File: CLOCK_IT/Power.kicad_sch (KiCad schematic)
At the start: 38 parts, among them SW1 CK_KMS2xxG, U4 AXP2101, U5 MC-264, U6 DS1338Z-NF, Y2 ABS07-32.768KHZ-T

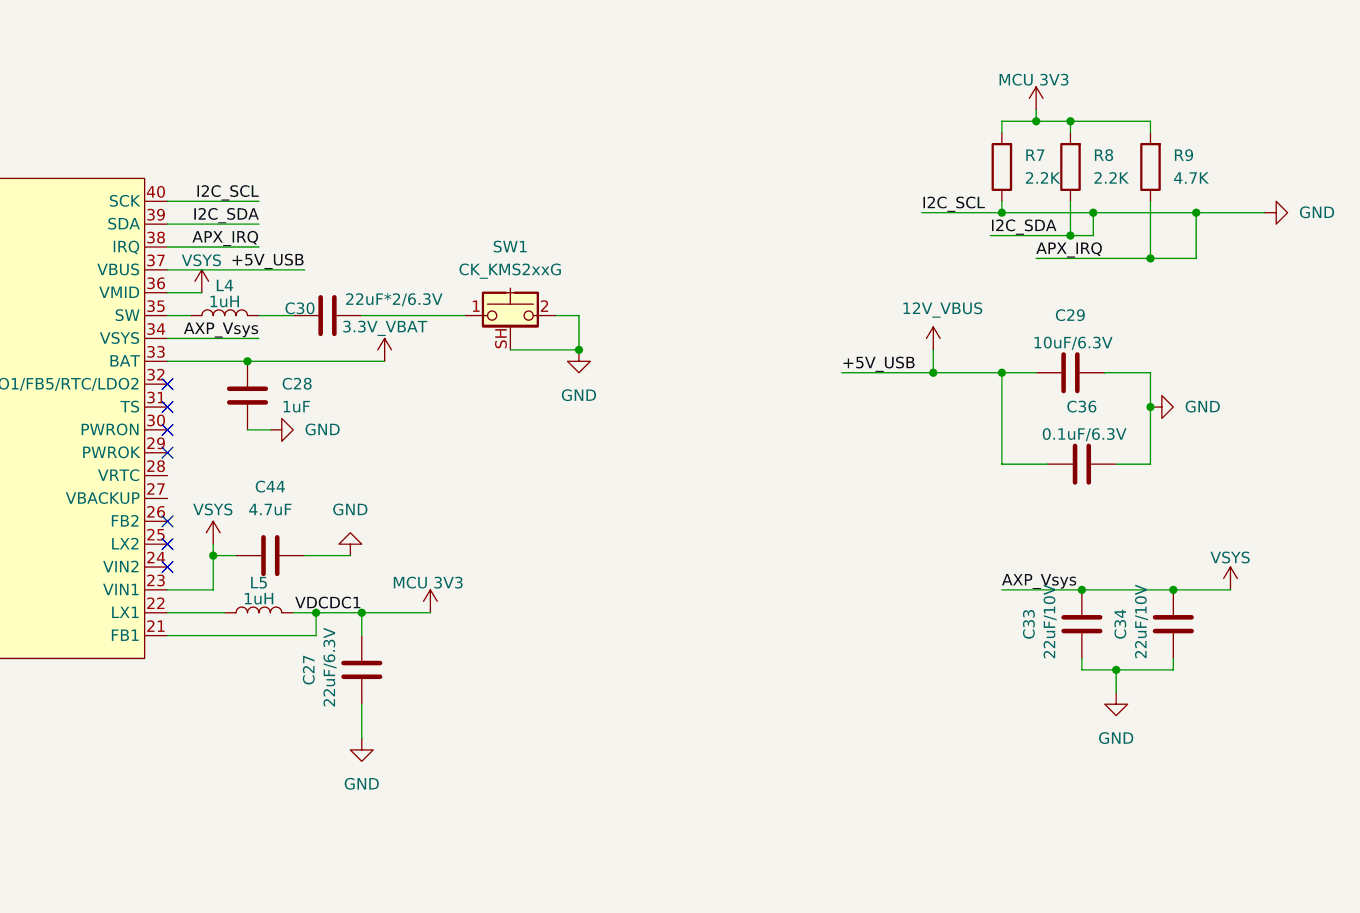
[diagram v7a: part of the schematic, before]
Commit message: :white_check_mark: CHANGES in 12C pull up resisors
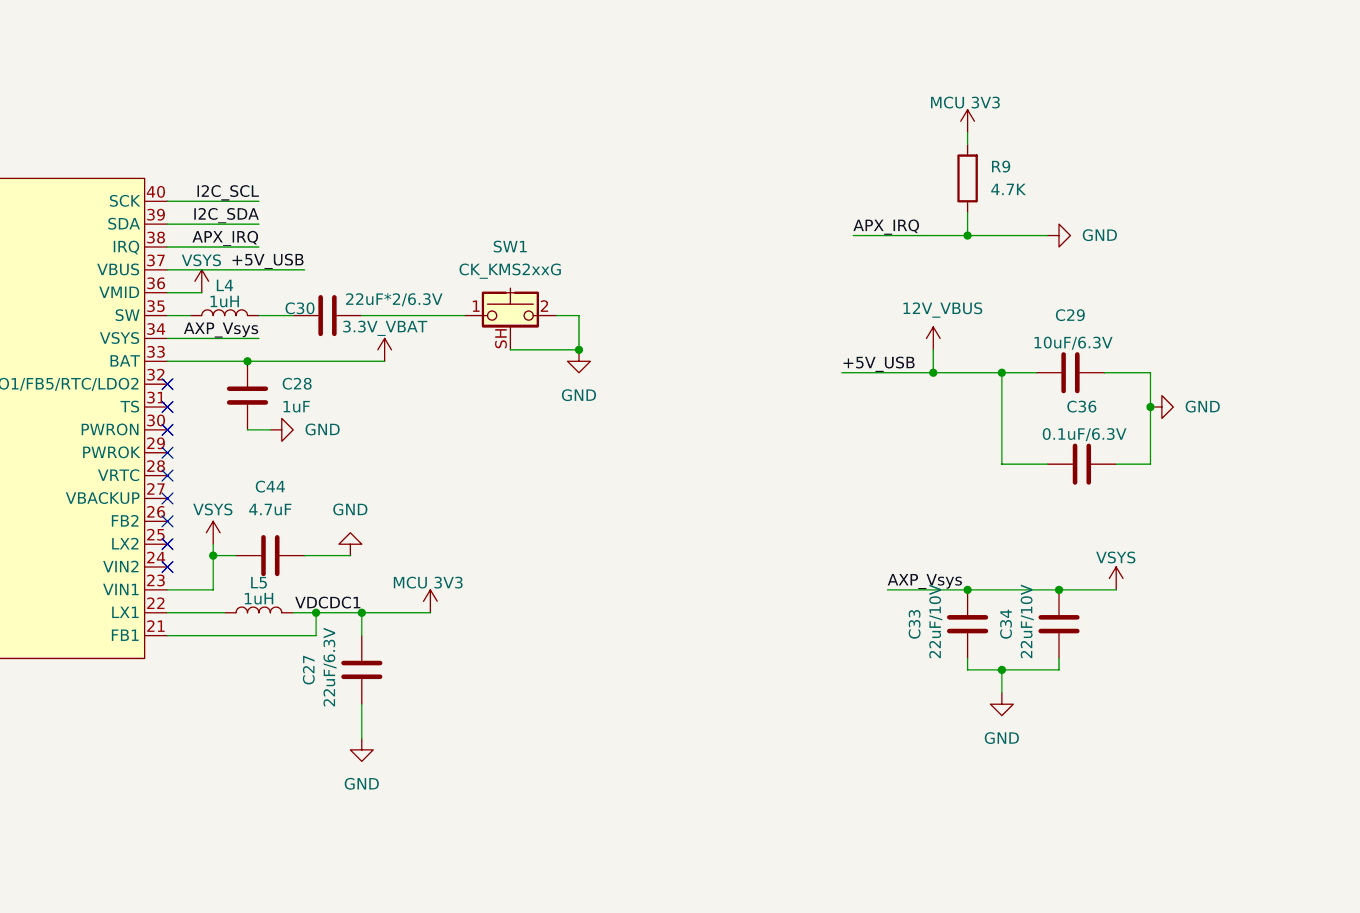
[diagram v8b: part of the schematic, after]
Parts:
- removed R7, R8: 2.2K, symbol Device:R
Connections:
- net GND: no longer U4.39 (SDA), U4.40 (SCK)
- new net I2C_SCL: U4.40 (SCK)
- new net I2C_SDA: U4.39 (SDA)
- no-connect marks 25 -> 27
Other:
- moved on the sheet: C33, C34, R9
